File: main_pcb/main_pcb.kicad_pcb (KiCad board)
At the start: 2 copper layers, 95 x 95 mm, 53 parts, among them J1 DBG, J2 UI, J3 UI, J4 Raspberry_Pi_Zero_WH, J5 UI, J6 UI, J7 UPDN, J8 ISP, J9 BTN_TRIG, Q1 BSS123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

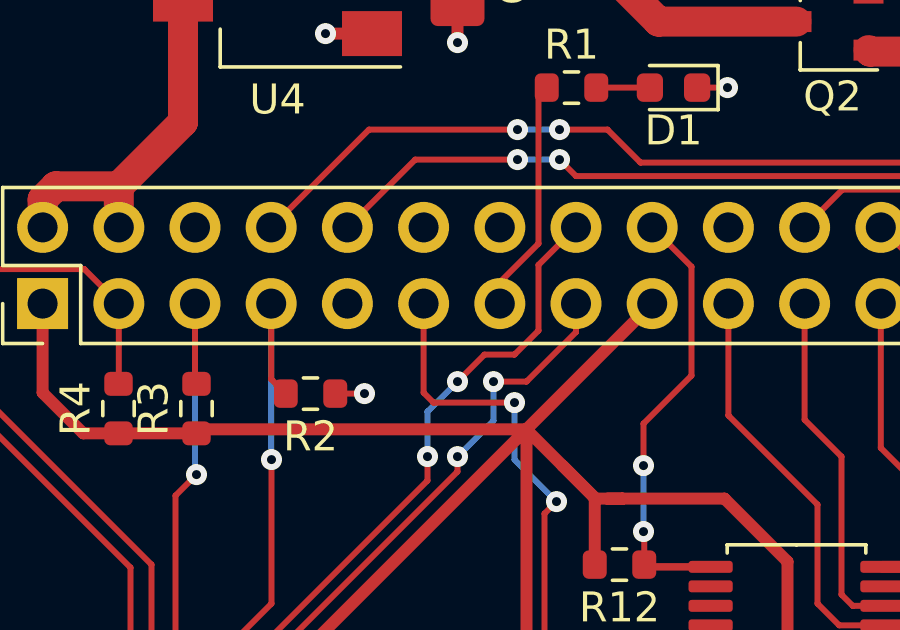
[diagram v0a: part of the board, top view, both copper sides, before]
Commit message: Switched SPI to CS0 on RPi
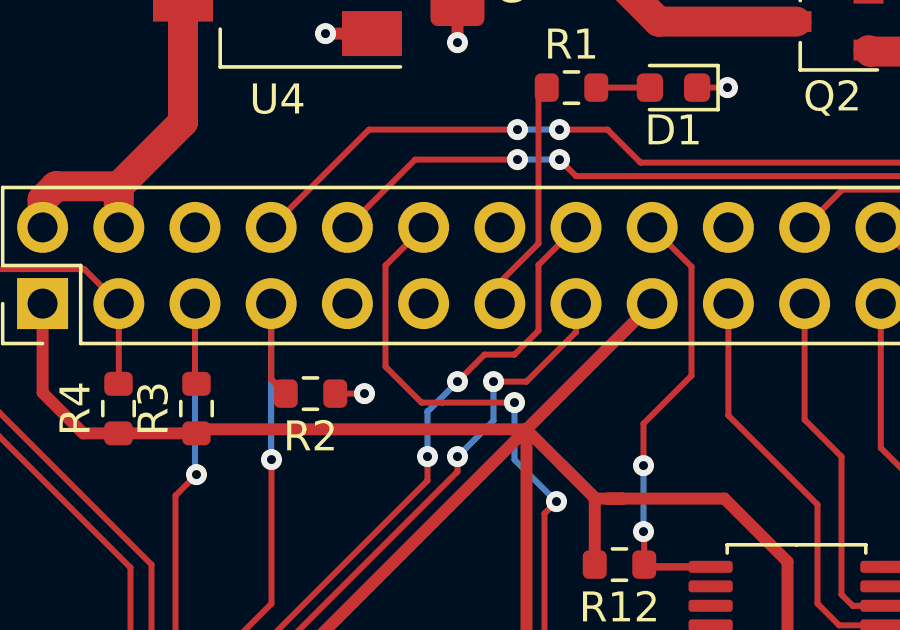
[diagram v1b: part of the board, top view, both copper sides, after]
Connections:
- J4 pad 11: /SS -> Net-(J4-Pad11)
- J4 pad 12: Net-(J4-Pad12) -> /SS
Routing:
- net /SS: track 107.5 -> 111.4 mm

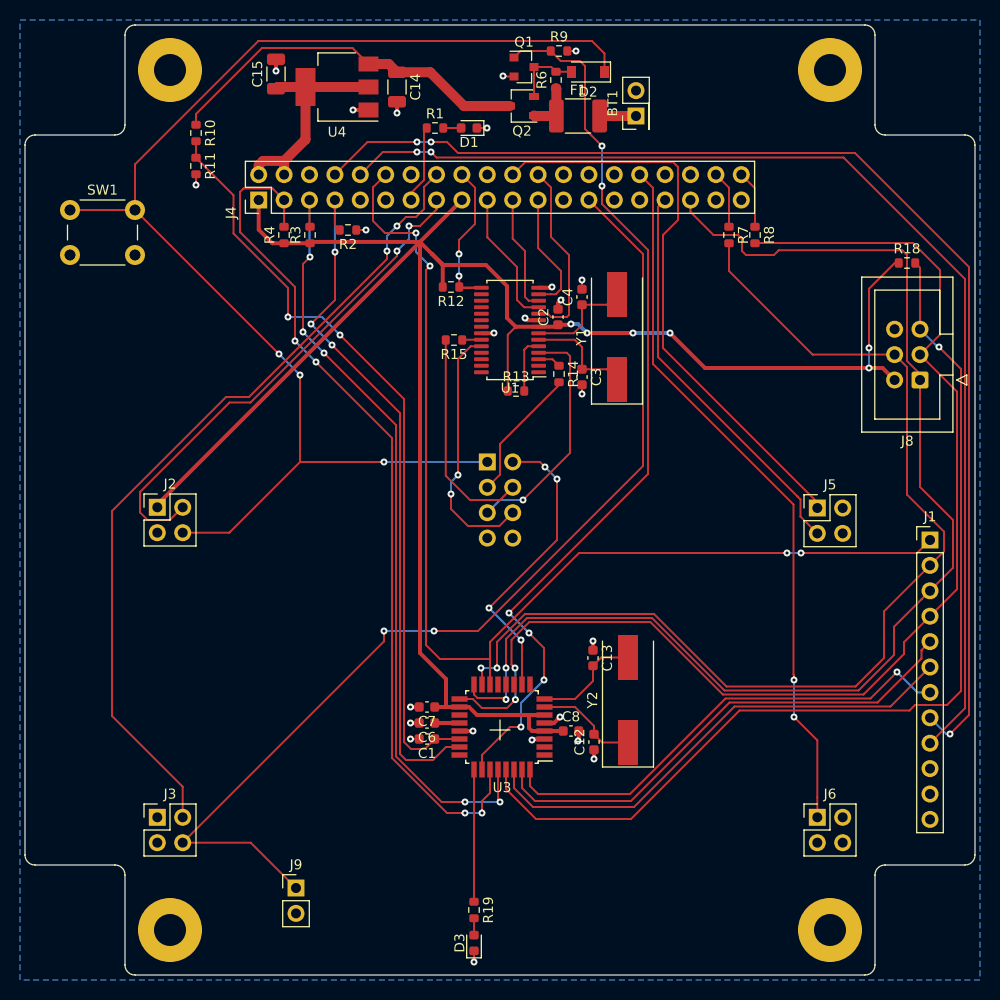
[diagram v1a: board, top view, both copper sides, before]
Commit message: Added MASTER_ON wire also to uC over a large resistor to detect button presses while powered on to turn off, cleaned silk screen
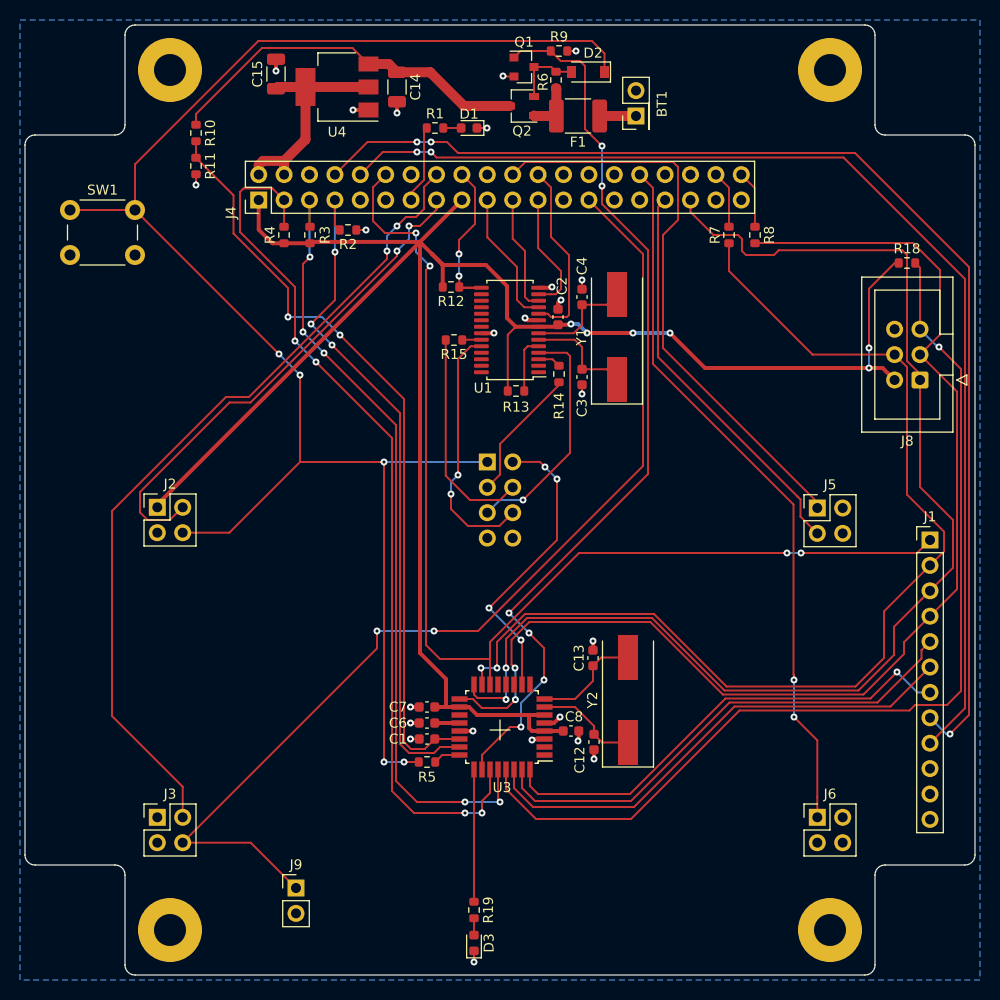
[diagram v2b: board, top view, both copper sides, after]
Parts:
- added R5: 100k, Resistor_SMD:R_0603_1608Metric, F.Cu at (142.7, 126.2)
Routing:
- net /MASTER_ON: track 130.9 -> 164.4 mm, vias 3 -> 5
- net Net-(R5-Pad2): track 0.00 -> 2.71 mm
- net /SDA: track 86.6 -> 88.5 mm
- net /SCL: track 78.1 -> 79.6 mm
- net /PI_SHTDN: track 70.0 -> 68.9 mm

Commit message: Added signal names to debug header on silk screen
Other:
- board text added: "GND"
- board text added: "MISO"
- board text added: "MOSI"
- board text added: "PD2"
- board text added: "PI_RXD"
- board text added: "PI_TXD"
- board text added: "SCK"
- board text added: "SS"
- board text added: "UC_RX"
- board text added: "UC_TX"

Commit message: Added comments for connector to modules on silk screen
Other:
- board text added: "DN_RETO"
- board text added: "DN_TX"
- board text added: "MASTER_ON"
- board text added: "NC"
- board text added: "TRIG"
- board text added: "UP_RETO"
- board text added: "UP_TX"

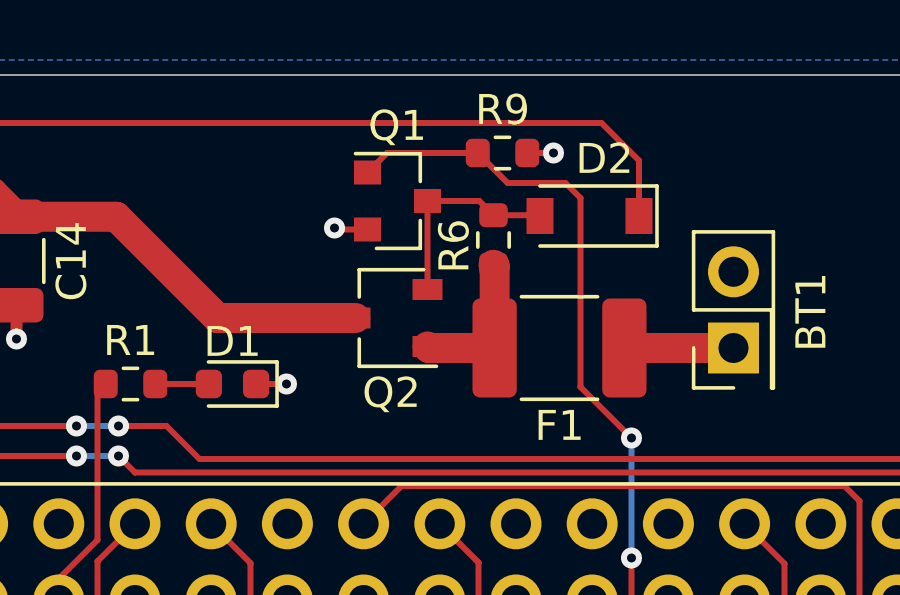
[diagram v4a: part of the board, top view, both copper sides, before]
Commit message: Fixed wrong pinout of p-channel mosfet for power control on main pcb and module pcb
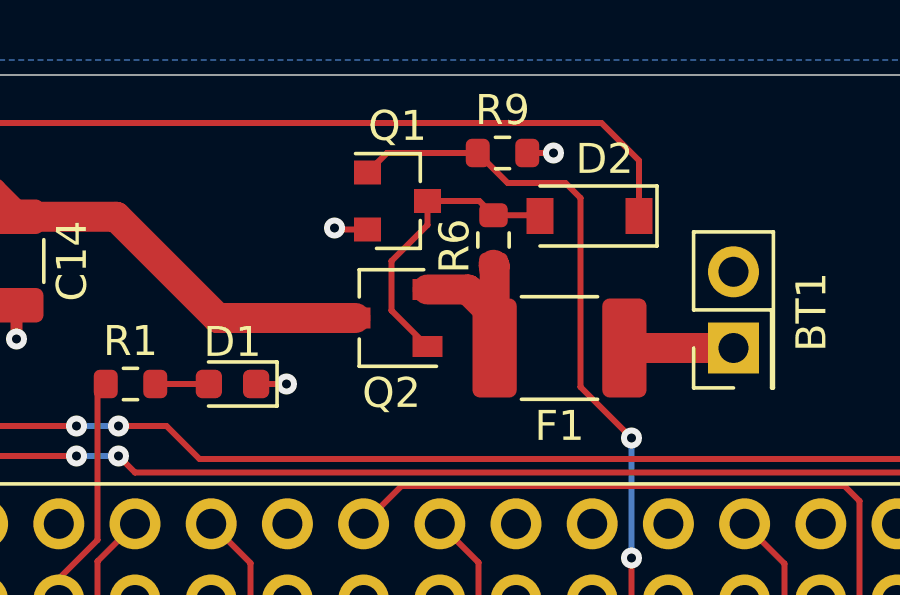
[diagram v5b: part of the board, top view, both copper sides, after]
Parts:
- Q2: value HSS2307 -> WTM2300
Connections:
- Q2 pad 1: /BAT_RAW -> Net-(D2-Pad2)
- Q2 pad 2: Net-(D2-Pad2) -> /BAT_RAW
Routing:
- net Net-(D2-Pad2): track 6.91 -> 9.80 mm

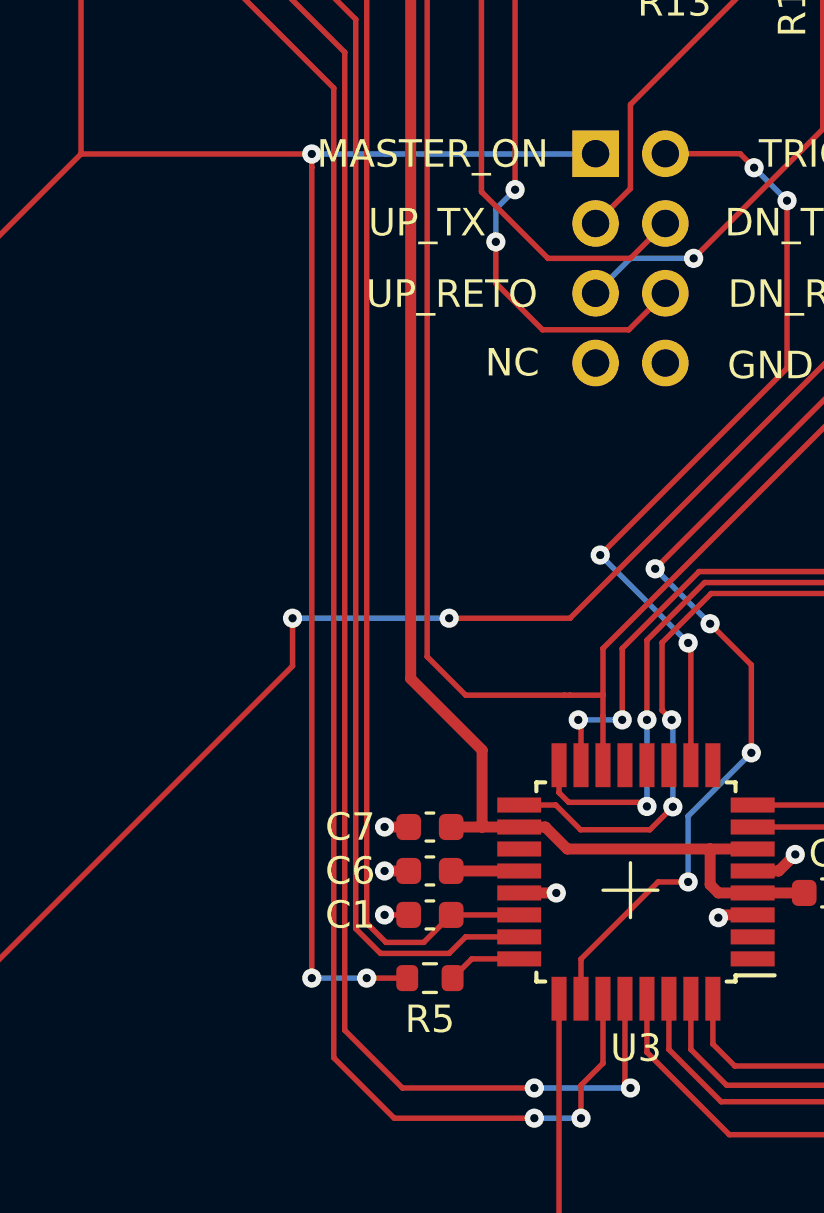
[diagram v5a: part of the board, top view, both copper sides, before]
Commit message: Modified resistor divider for power measurement, replaced resistor with diode for master button input
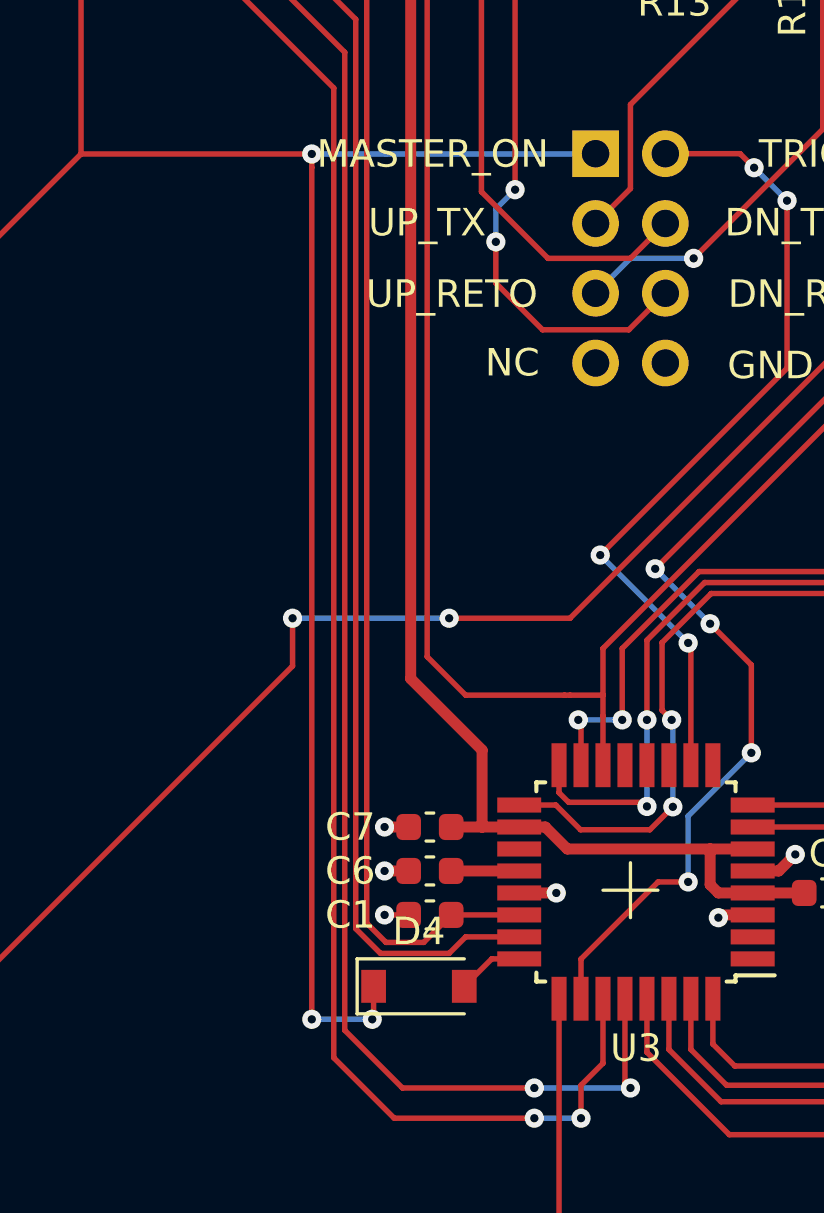
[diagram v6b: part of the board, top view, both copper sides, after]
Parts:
- removed R5: 100k, Resistor_SMD:R_0603_1608Metric
- added D4: D_Schottky, Diode_SMD:D_SOD-123, F.Cu at (142.3, 126.5)
- Q2: value WTM2300 -> HSS2307
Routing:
- net /MASTER_ON: track 164.4 -> 165.8 mm

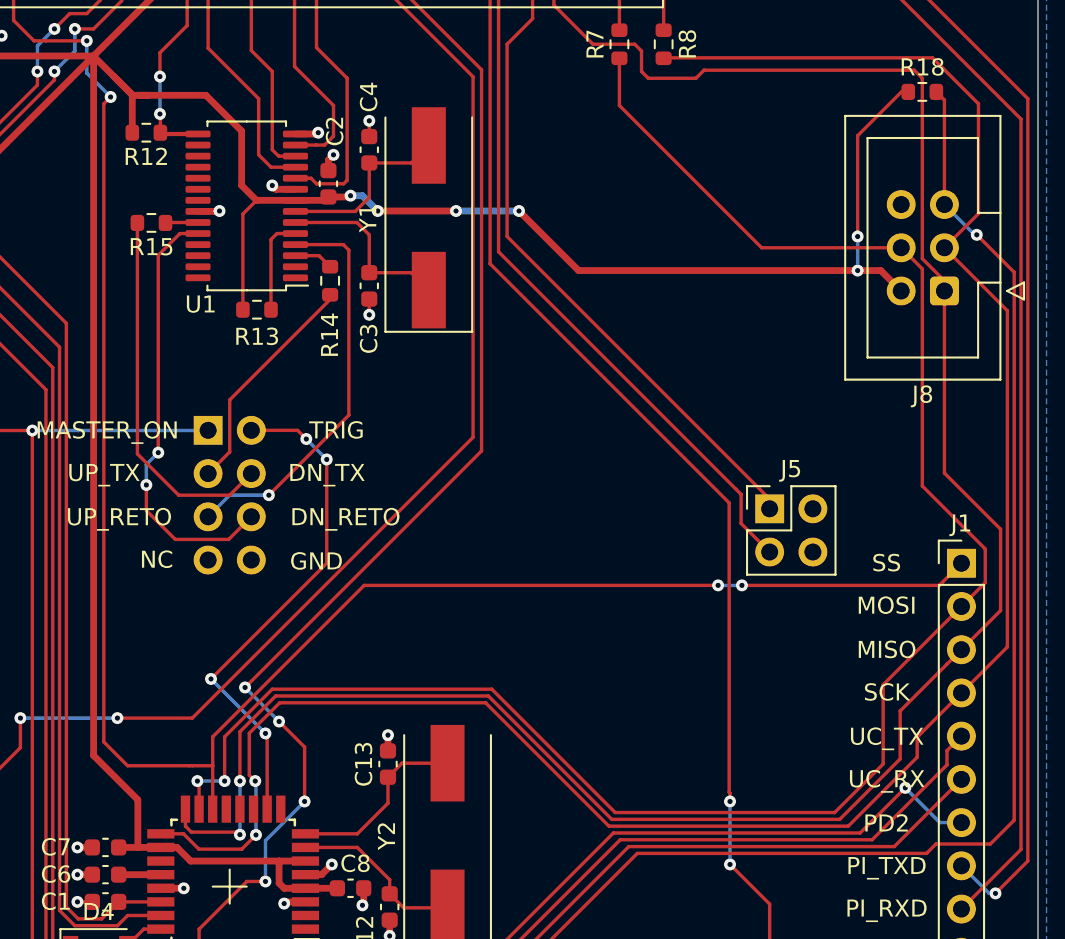
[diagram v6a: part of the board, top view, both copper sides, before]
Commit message: Moved TRIG wire on a different pin to use timer1 instead of timer0 to have a 16 bit timer, which is also already implemented in the firmware
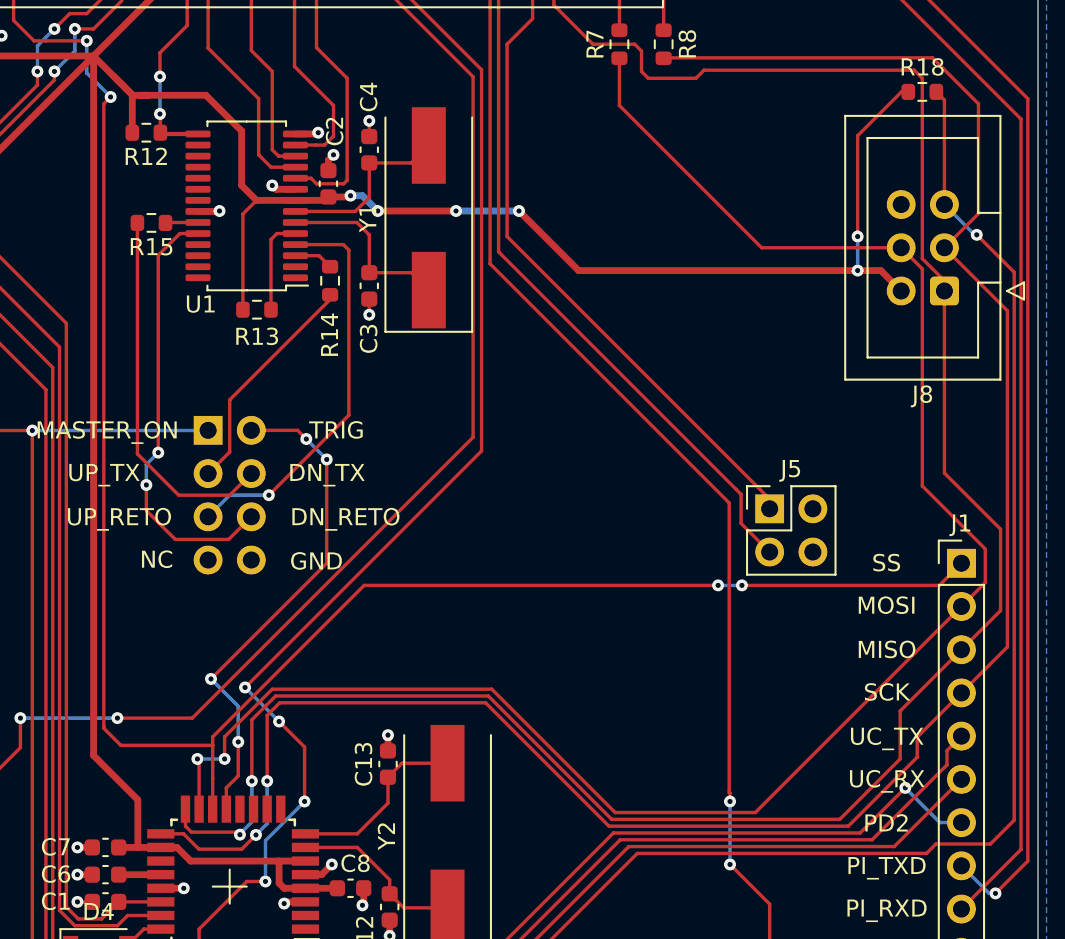
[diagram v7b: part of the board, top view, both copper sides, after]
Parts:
- R10: value 10k -> 68k
- R11: value 15k -> 10k
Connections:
- U3 pad 10: /TRIG -> Net-(U3-Pad10)
- U3 pad 13: Net-(U3-Pad13) -> /TRIG
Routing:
- net /MOSI: track 107.6 -> 104.9 mm
- net /SS: track 111.4 -> 110.4 mm
